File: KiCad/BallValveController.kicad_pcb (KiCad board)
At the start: 2 copper layers, 55.6 x 43.2 mm, 47 parts, among them J1 Screw_Terminal_01x03, J10 Screw_Terminal_01x04, J11 Screw_Terminal_01x02, J2 Screw_Terminal_01x04, J3 Screw_Terminal_01x04, J4 Screw_Terminal_01x04, J5 Conn_01x01_Male, J6 Conn_01x01_Male, J7 Conn_01x01_Male, J8 Conn_01x01_Male, J9 Conn_01x01_Male, K1 G5V-2, Q1 Q_PMOS_GDS, Q2 2N2222A, U1 L7805, U3 XIAO-ESP32-C6

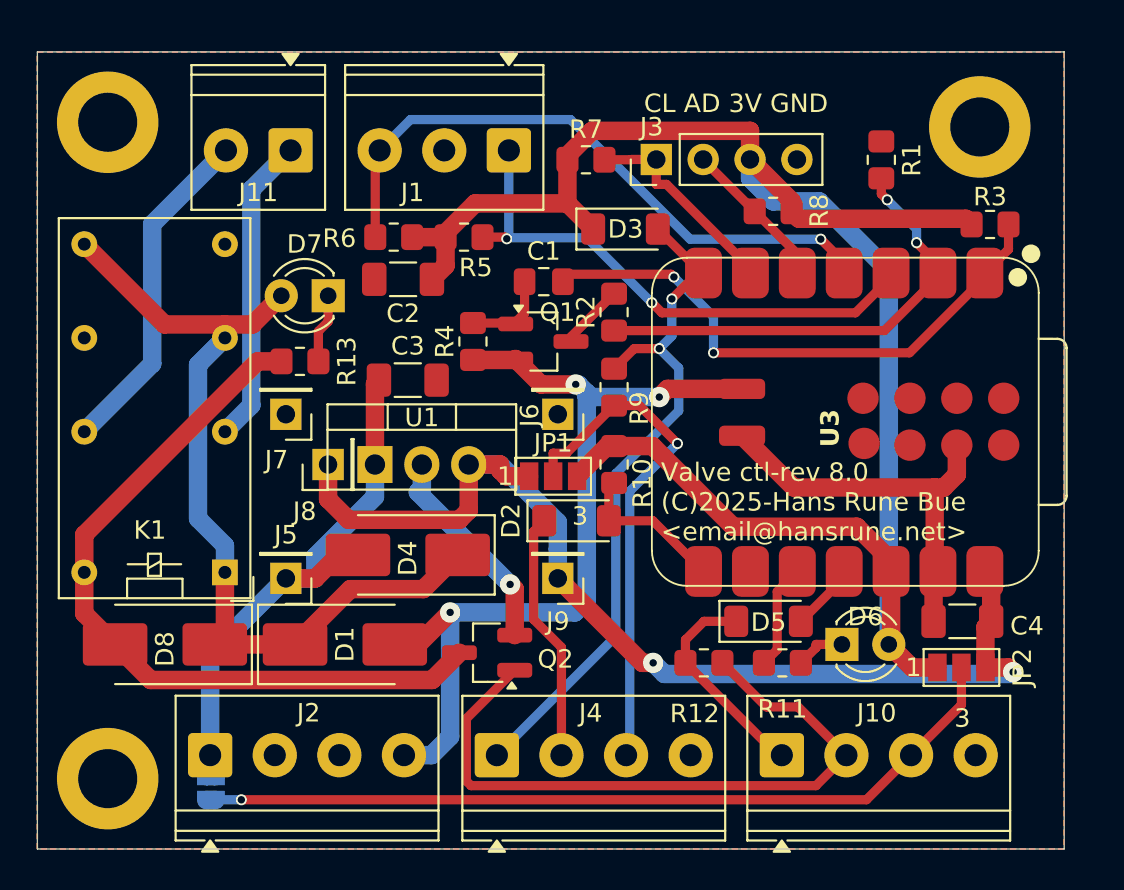
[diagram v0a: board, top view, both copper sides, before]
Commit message: Added step down converter
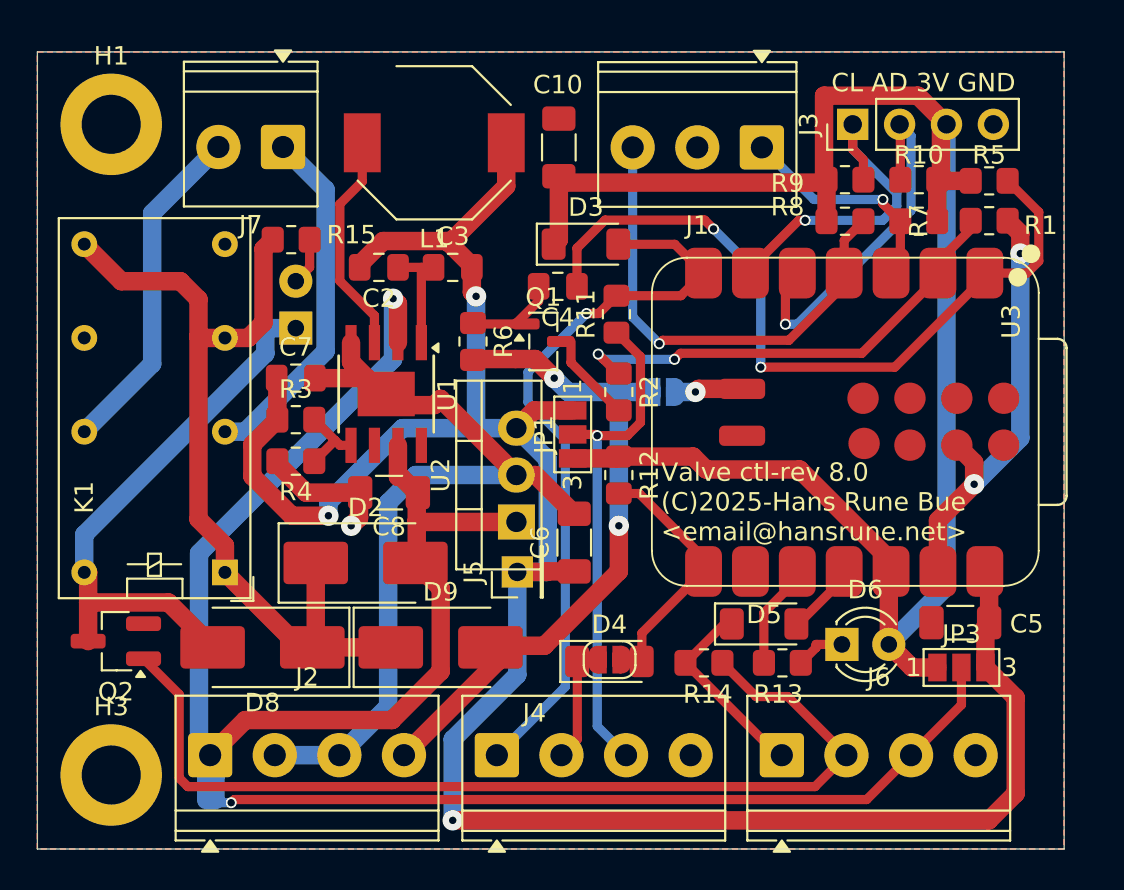
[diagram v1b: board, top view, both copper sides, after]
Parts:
- removed the C4 at (186.0, 112.0)
- removed D1: 1N4007, Diode_SMD:D_SMB_Handsoldering
- removed the H3 at (186.9, 85.2)
- removed the J5 at (149.4, 109.7)
- removed the J6 at (164.1, 100.8)
- removed the J7 at (149.4, 100.8)
- removed J9: Conn_01x01_Male, Connector_PinHeader_2.54mm:PinHeader_1x01_P2.54mm_Vertical
- added C2: 100nF, Capacitor_SMD:C_0805_2012Metric_Pad1.18x1.45mm_HandSolder, F.Cu at (154.4, 92.8)
- added C5: 22uF, Capacitor_SMD:C_1206_3216Metric_Pad1.33x1.80mm_HandSolder, F.Cu at (185.9, 112.1)
- added C6: 22uF, Capacitor_SMD:C_1206_3216Metric_Pad1.33x1.80mm_HandSolder, F.Cu at (165.0, 107.7)
- added C7: 100nF, Capacitor_SMD:C_0805_2012Metric_Pad1.18x1.45mm_HandSolder, F.Cu at (149.9, 98.8)
- added C8: 22uF, Capacitor_SMD:C_1206_3216Metric_Pad1.33x1.80mm_HandSolder, F.Cu at (154.9, 105.0)
- added D9: 1N4007, Diode_SMD:D_SMB_Handsoldering, F.Cu at (157.7, 113.4)
- added JP4: SolderJumper_2_Open, Jumper:SolderJumper-2_P1.3mm_Open_RoundedPad1.0x1.5mm, F.Cu at (166.9, 114.1)
- added JP5: SolderJumper_2_Open, Jumper:SolderJumper-2_P1.3mm_Open_RoundedPad1.0x1.5mm, B.Cu at (169.8, 99.6)
- added L1: L, Inductor_SMD:L_Bourns-SRU8028_8.0x8.0mm, F.Cu at (157.4, 86.1)
- added R3: 88k7, Resistor_SMD:R_0805_2012Metric_Pad1.20x1.40mm_HandSolder, F.Cu at (149.9, 101.1)
- added R4: 20k, Resistor_SMD:R_0805_2012Metric_Pad1.20x1.40mm_HandSolder, F.Cu at (149.9, 103.3)
- added U1: MT2499A, Package_SO:TI_SO-PowerPAD-8, F.Cu at (154.8, 99.7)
- C3: value 10uF -> 22nF; footprint Capacitor_SMD:C_1206_3216Metric_Pad1.33x1.80mm_HandSolder -> Capacitor_SMD:C_0805_2012Metric_Pad1.18x1.45mm_HandSolder
- D7: moved to B.Cu
- Q1: footprint Package_TO_SOT_SMD:SOT-23_Handsoldering -> Package_TO_SOT_SMD:SOT-23
- moved R7 24.7 mm to (183.6, 90.3), turned to 180 degrees
- moved R8 24.5 mm to (179.6, 90.3), turned to 0 degrees
- moved Q2 20.1 mm to (140.1, 113.1)
- moved R9 14.1 mm to (179.6, 88.1)
- moved J1 13.7 mm to (175.1, 86.3)
- moved J5 11.8 mm to (161.9, 109.3)
- moved C10 11.1 mm to (164.1, 86.3), turned to 90 degrees
- moved J3 10.8 mm to (180.1, 85.1)
- moved U2 8.27 mm to (161.8, 106.6), turned to 90 degrees
- moved R10 8.07 mm to (183.6, 88.1)
- moved D4 7.82 mm to (166.9, 114.2)
- moved R1 6.71 mm to (187.5, 90.3), turned to 180 degrees
- moved R15 6.61 mm to (149.6, 91.3), turned to 180 degrees
- moved C3 6.58 mm to (158.4, 92.8)
- moved D8 5.28 mm to (148.1, 113.4)
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- renumbered C2 to C10, C1 to C4, D4 to D2, D2 to D4, H4 to H3, J8 to J5, J10 to J6, J11 to J7, JP4 to JP2, JP2 to JP3, R8 to R10, R9 to R11, R10 to R12, R11 to R13, R12 to R14, R13 to R15, R3 to R5, R4 to R6, R5 to R7, R6 to R8, R7 to R9, U1 to U2
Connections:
- C3 pad 1: /PwrIn -> Net-(U1-BS)
- C3 pad 2: GND -> +5V
- D7 pad 1: Net-(D7-K) -> /RELAYSW
- D7 pad 2: +VSW -> Net-(D7-A)
- R15 pad 1: /RELAYSW -> Net-(D7-A)
- R15 pad 2: Net-(D7-K) -> +VSW
- U3 pad 15: /VBAT -> /JPBAT
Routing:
- net +5V: track 59.5 -> 122.0 mm, vias 2 -> 3
- net GND: track 33.6 -> 74.7 mm, vias 1 -> 3
- net /PwrIn: track 29.5 -> 66.1 mm, vias 0 -> 1
- net /VOPEN: track 29.6 -> 12.3 mm, vias 2 -> 1
- net /ILow: track 37.3 -> 53.1 mm
- net Net-(U1-SW): track 0.00 -> 12.1 mm
- net /SDA: track 8.27 -> 20.3 mm, vias 0 -> 1
- net /VBAT: track 47.8 -> 36.4 mm, vias 3 -> 2
- net /RELAYSW: track 41.3 -> 30.4 mm
- net Net-(U3-GPIO0_A0_D0): track 31.0 -> 41.5 mm
- net /VCLOSE: track 34.4 -> 26.5 mm
- net /RX: track 13.6 -> 6.63 mm
- net /SCL: track 11.4 -> 18.2 mm, vias 0 -> 1
- net Net-(U1-BS): track 0.00 -> 6.00 mm
- net Net-(D4-A): track 8.43 -> 14.0 mm
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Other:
- board text added: "M2 M1"
- board text added: "VO GND VC"
- board text removed: "VO GND VC M2 M1"

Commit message: New diode footprints
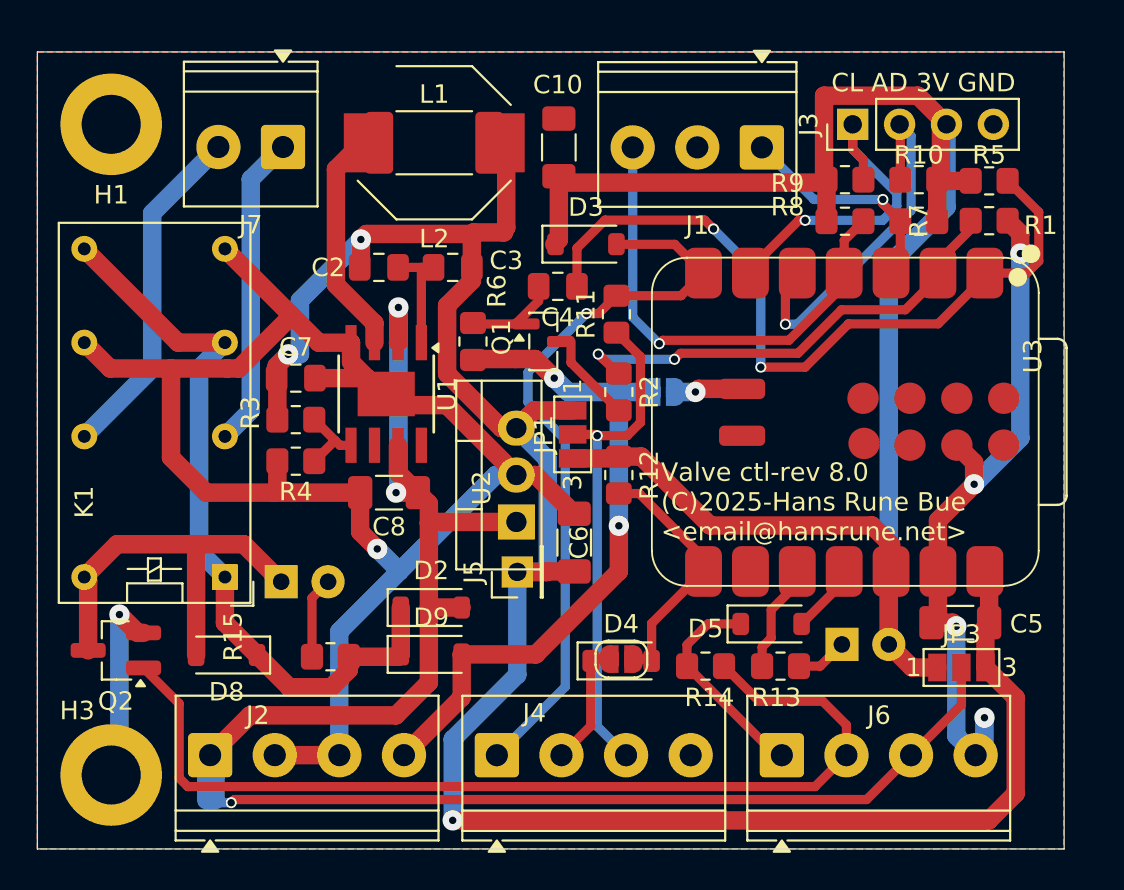
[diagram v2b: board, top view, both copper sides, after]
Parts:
- added L2: L, Inductor_SMD:L_Bourns-SRU8028_8.0x8.0mm, F.Cu at (157.4, 86.1)
- D2, D8, D9: footprint Diode_SMD:D_SMB_Handsoldering -> Diode_SMD:D_SOD-123
- D3, D4, D5: footprint Diode_SMD:D_MiniMELF -> Diode_SMD:D_SOD-123
- D6: moved to B.Cu
- L1: footprint Inductor_SMD:L_Bourns-SRU8028_8.0x8.0mm -> Inductor_SMD:L_2512_6332Metric_Pad1.52x3.35mm_HandSolder
- moved R15 22.7 mm to (151.8, 113.9), turned to 0 degrees
- moved D7 13.8 mm to (149.1, 109.9), turned to 0 degrees
- moved D2 4.30 mm to (157.2, 111.3)
- moved D8 1.99 mm to (146.1, 113.8)
- moved D4 0.64 mm to (167.5, 114.1)
- moved JP4 0.64 mm to (167.5, 114.0)
- moved D9 0.64 mm to (157.2, 113.8)
- moved Q2 0.50 mm to (140.1, 113.6)
- moved D5 0.38 mm to (175.6, 112.1)
- moved K1 0.25 mm to (146.1, 109.6)
- moved R13 0.20 mm to (176.1, 114.4)
- moved R14 0.20 mm to (172.1, 114.4)
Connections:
- net Net-(U1-SW) renamed /IND1
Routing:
- net GND: track 74.7 -> 133.9 mm, vias 3 -> 6
- net /PwrIn: track 66.1 -> 47.9 mm, vias 1 -> 2
- net /RELAYSW: track 30.4 -> 22.3 mm
- net +5V: track 122.0 -> 115.1 mm
- net +VSW: track 46.8 -> 40.7 mm
- net /MOTOR2: track 19.3 -> 17.0 mm
- net Net-(D7-A): track 2.56 -> 4.43 mm
- net /VBAT: track 36.4 -> 37.3 mm
- net /IHigh: track 11.0 -> 11.7 mm
- net +3V3: track 96.3 -> 96.9 mm

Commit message: Footprint change 1N4148 to SOD-323
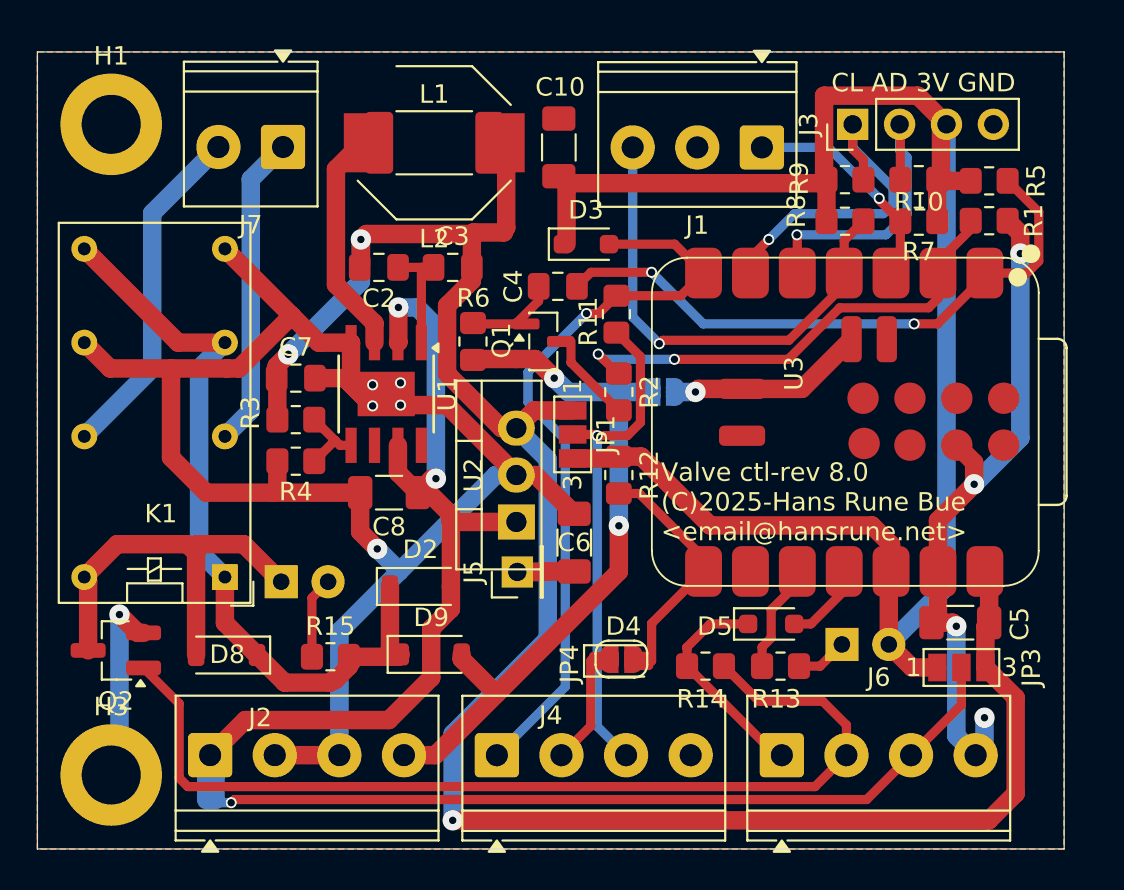
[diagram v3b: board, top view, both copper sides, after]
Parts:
- D3, D4, D5: footprint Diode_SMD:D_SOD-123 -> Diode_SMD:D_SOD-323_HandSoldering
- U3: footprint LOCAL1:XIAO-ESP32-C6-SMD -> LOCAL1:XIAO-ESP32-C3C6-SMD
- moved D2 1.28 mm to (156.6, 110.1)
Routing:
- net Net-(U3-GPIO0_A0_D0): track 41.5 -> 33.1 mm
- net /JPBAT: track 3.70 -> 10.7 mm
- net /SDA: track 20.3 -> 16.6 mm
- net GND: track 133.9 -> 135.7 mm, vias 6 -> 10
- net /VBAT: track 37.3 -> 38.8 mm
- net +VSW: track 40.7 -> 41.8 mm
- net /PwrIn: track 47.9 -> 46.9 mm
- net Net-(D5-A): track 3.80 -> 4.70 mm
- net /TX: track 40.1 -> 40.8 mm
- net Net-(U3-GPIO1_A1_D1): track 25.7 -> 26.4 mm
- net +3V3: track 96.9 -> 97.5 mm
- net /IHigh: track 11.7 -> 12.2 mm

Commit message: New layout - changed Diodes and Cap footprints + RX/TX wiring
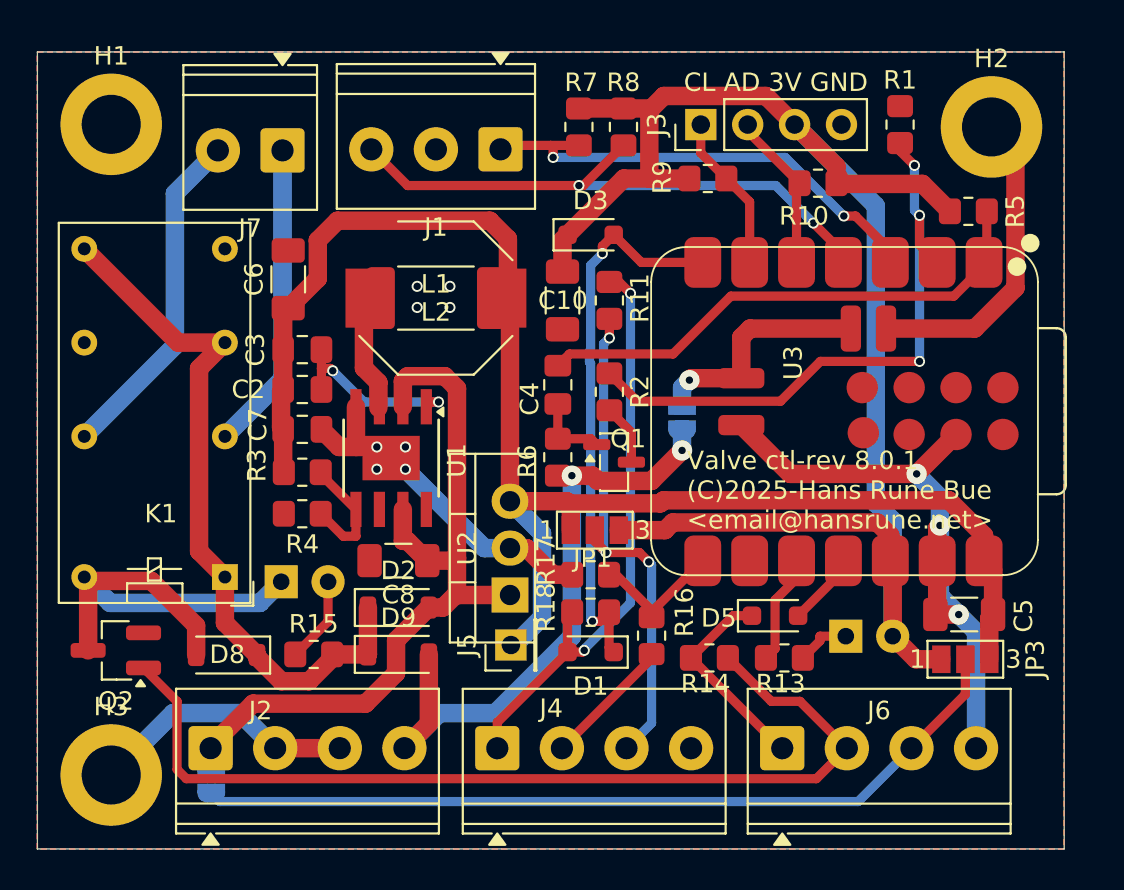
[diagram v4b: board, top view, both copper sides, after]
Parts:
- removed D4: 1N4148, Diode_SMD:D_SOD-323_HandSoldering
- removed JP4: SolderJumper_2_Open, Jumper:SolderJumper-2_P1.3mm_Open_RoundedPad1.0x1.5mm
- removed R12: 4.7k, Resistor_SMD:R_0805_2012Metric_Pad1.20x1.40mm_HandSolder
- added D1: 1N4148, Diode_SMD:D_SOD-323_HandSoldering, F.Cu at (165.9, 113.7)
- added H2: MountingHole_Pad, MountingHole:MountingHole_3.2mm_M3_ISO14580_Pad, F.Cu at (187.6, 85.2)
- added R16: 2.2k, Resistor_SMD:R_0805_2012Metric_Pad1.20x1.40mm_HandSolder, F.Cu at (169.2, 112.8)
- added R17: 4.3k, Resistor_SMD:R_0805_2012Metric_Pad1.20x1.40mm_HandSolder, F.Cu at (165.9, 109.5)
- added R18: 0, Resistor_SMD:R_0805_2012Metric_Pad1.20x1.40mm_HandSolder, F.Cu at (165.9, 111.5)
- moved C6 21.1 mm to (149.5, 93.5)
- moved R7 19.1 mm to (165.2, 85.2), turned to -90 degrees
- moved J1 14.2 mm to (161.0, 86.4)
- moved R8 13.0 mm to (167.6, 85.2), turned to -90 degrees
- moved C3 9.29 mm to (150.2, 97.3), turned to 180 degrees
- moved L1 8.41 mm to (157.5, 94.5)
- moved L2 8.41 mm to (157.5, 94.5)
- moved C10 8.29 mm to (164.3, 94.6), turned to -90 degrees
- moved J3 8.23 mm to (171.8, 85.1)
- moved C2 7.81 mm to (150.2, 99.4)
- moved R6 7.77 mm to (164.1, 103.1)
- moved Q1 7.58 mm to (167.1, 103.4)
- moved R9 7.43 mm to (172.2, 88.0)
- moved R1 7.10 mm to (182.6, 85.1), turned to -90 degrees
- moved R10 5.46 mm to (178.2, 88.3)
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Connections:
- D3 pad 2: /TX -> Net-(D1-K)
- U3 pad 7: /TX -> Net-(D1-K)
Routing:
- net GND: track 135.7 -> 90.2 mm, vias 10 -> 11
- net +5V: track 115.5 -> 84.2 mm, vias 3 -> 0
- net Net-(D1-K): track 0.00 -> 30.4 mm, vias 0 -> 2
- net /VOPEN: track 12.2 -> 26.0 mm, vias 1 -> 2
- net /SCL: track 18.2 -> 8.56 mm, vias 1 -> 0
- net /TX: track 40.8 -> 31.8 mm, vias 1 -> 2
- net /SDA: track 16.6 -> 8.70 mm, vias 1 -> 0
- net Net-(U3-GPIO1_A1_D1): track 26.4 -> 33.5 mm, vias 2 -> 3
- net +3V3: track 97.5 -> 91.1 mm
- net Net-(U3-GPIO17_D7_RX): track 13.8 -> 7.47 mm
- net /VCLOSE: track 26.5 -> 31.7 mm, vias 1 -> 2
- net /PwrIn: track 46.9 -> 41.8 mm, vias 2 -> 0
- net Net-(U3-GPIO0_A0_D0): track 33.1 -> 28.3 mm, vias 2 -> 0
- net /IND1: track 12.3 -> 7.82 mm
- net /VBAT: track 38.8 -> 34.6 mm
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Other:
- board text added: "Valve ctl-rev 8.0.1 (C)2025-Hans Rune Bue <email@hansrune.net>"
- board text removed: "Valve ctl-rev 8.0 (C)2025-Hans Rune Bue <email@hansrune.net>"

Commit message: Version 8.0.2 pdf files
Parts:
- added TP1: TestPoint, TestPoint:TestPoint_THTPad_D1.0mm_Drill0.5mm, F.Cu at (162.1, 99.9)
- added TP2: TestPoint, TestPoint:TestPoint_THTPad_D1.0mm_Drill0.5mm, F.Cu at (160.1, 100.3)
- added TP3: TestPoint, TestPoint:TestPoint_THTPad_D1.0mm_Drill0.5mm, F.Cu at (182.1, 89.9)
- added TP4: TestPoint, TestPoint:TestPoint_THTPad_D1.0mm_Drill0.5mm, F.Cu at (148.5, 111.6)
- added TP5: TestPoint, TestPoint:TestPoint_THTPad_D1.0mm_Drill0.5mm, F.Cu at (148.6, 108.0)
- added TP6: TestPoint, TestPoint:TestPoint_THTPad_D1.0mm_Drill0.5mm, F.Cu at (162.1, 102.0)
- Q2: footprint Package_TO_SOT_SMD:SOT-23_Handsoldering -> Package_TO_SOT_SMD:SOT-23
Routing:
- net +VSW: track 38.5 -> 41.7 mm
- net /VBAT: track 34.6 -> 37.6 mm
- net Net-(Q1-G): track 4.13 -> 6.27 mm
- net +5V: track 84.2 -> 85.5 mm
- net /RELAYSW: track 24.2 -> 25.1 mm
- net +3V3: track 91.1 -> 91.9 mm
- net Net-(U3-GPIO0_A0_D0): track 28.3 -> 29.0 mm
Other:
- board text added: "Valve ctl-rev 8.0.2 (C)2025-Hans Rune Bue <email@hansrune.net>"
- board text removed: "Valve ctl-rev 8.0.1 (C)2025-Hans Rune Bue <email@hansrune.net>"
